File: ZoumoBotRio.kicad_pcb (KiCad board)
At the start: 2 copper layers, 89.7 x 54.9 mm, 148 parts, among them CON1 BARREL_JACK, J1 Screw_Terminal_1x05, J2 Screw_Terminal_1x05, P1 USB_OTG, P10 Analog, P11 Digital, P12 Analog, P13 Digital, P14 CONN_01X06, P2 Analog, P3 Digital, P4 Analog, P5 Digital, P6 Analog, P7 Digital, P8 Analog, P9 Digital, Q1 Q_PMOS_GDS, Q2 IR Receiver, Q3 IR Receiver, U1 ZLDO1117K50TC, U2 ATmega32U4-AU, U3 SOT361-1_2, U4 TB6612FNG, U5 TB6612FNG, Y1 16MHz

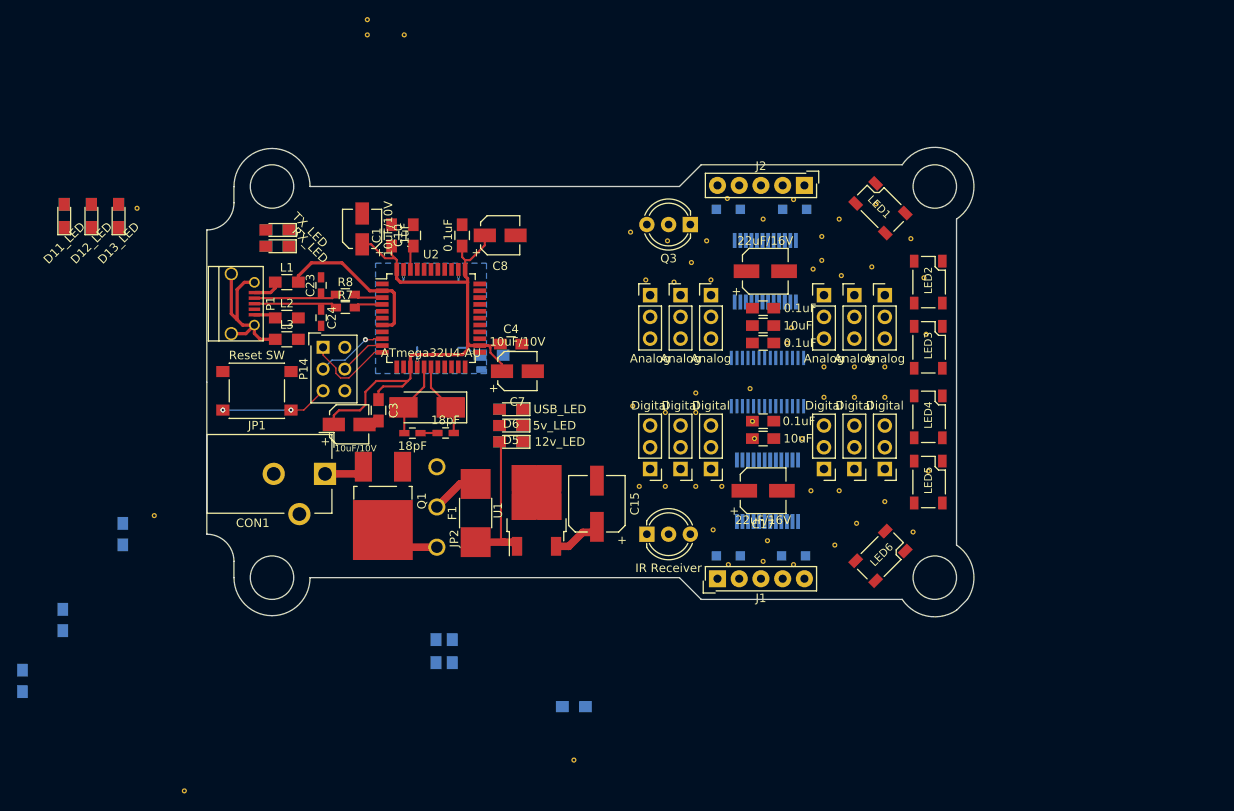
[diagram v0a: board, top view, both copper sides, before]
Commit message: Finished v2 layout, no traces
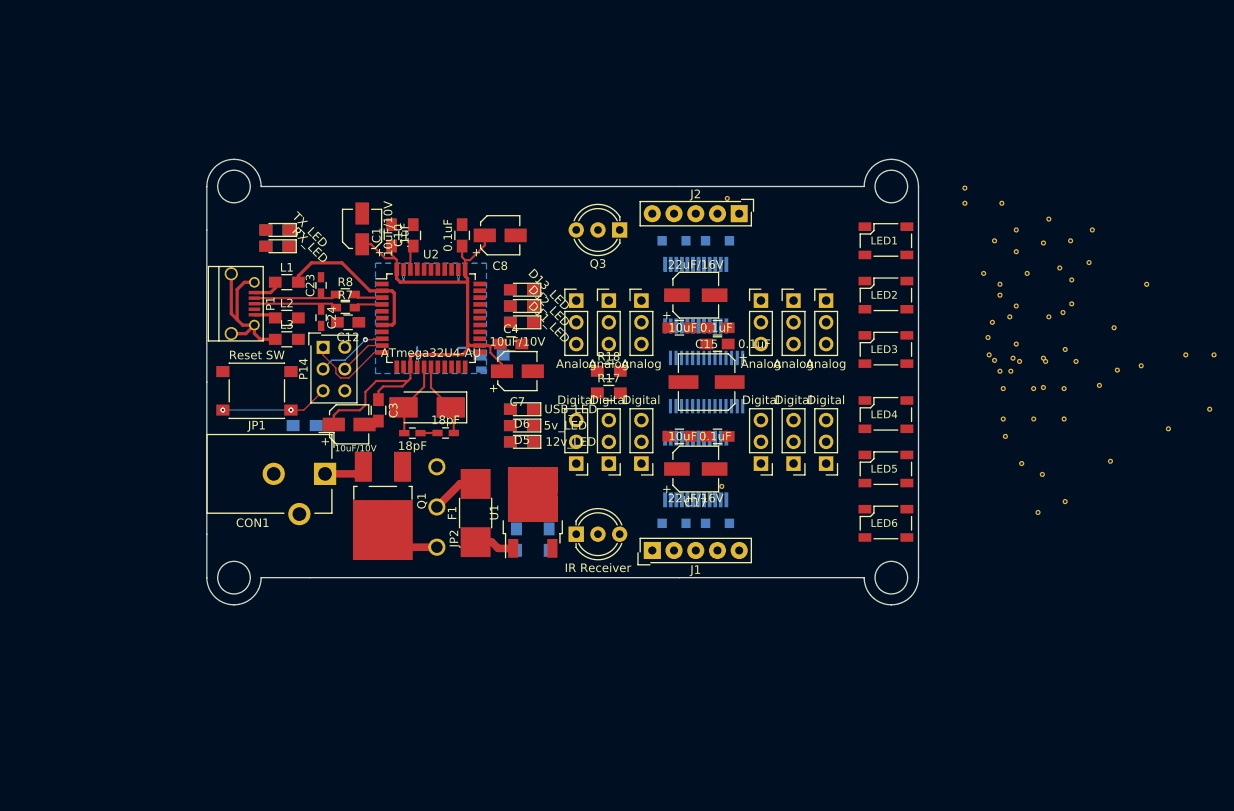
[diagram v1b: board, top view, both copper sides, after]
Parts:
- C12, R17, R18: moved to F.Cu
- moved REF** 117.0 mm to (208.5, 112.2), turned to 45 degrees
- moved REF** 111.9 mm to (209.8, 121.0)
- moved REF** 109.7 mm to (204.5, 108.0)
- moved REF** 80.9 mm to (210.2, 105.4), turned to 45 degrees
- moved REF** 72.6 mm to (197.1, 90.9)
- moved REF** 72.6 mm to (192.8, 90.9)
- moved REF** 72.6 mm to (192.8, 89.1)
- moved C14 63.7 mm to (144.1, 130.2)
- moved D4 54.9 mm to (141.0, 104.8), turned to 180 degrees
- moved R5 54.9 mm to (141.0, 104.8), turned to 180 degrees
- moved C13 53.9 mm to (140.3, 130.2)
- moved REF** 51.4 mm to (205.1, 95.2)
- moved D3 51.4 mm to (141.0, 102.9), turned to 180 degrees
- moved R4 51.4 mm to (141.0, 102.9), turned to 180 degrees
- moved REF** 49.8 mm to (213.4, 109.9)
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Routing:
- net +12V: track 16.4 -> 4.94 mm
- net +5V: track 75.2 -> 69.5 mm
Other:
- board size 89.7 x 54.9 mm -> 83.2 x 52.1 mm

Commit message: Started drawing traces
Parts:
- moved REF** 28.5 mm to (193.2, 94.6)
- moved R18 2.54 mm to (151.2, 113.0)
- moved D2 2.54 mm to (141.0, 98.4)
- moved R3 2.54 mm to (141.0, 98.4)
- moved R17 1.91 mm to (151.2, 111.1)
- moved D3 1.27 mm to (141.0, 101.6)
- moved R4 1.27 mm to (141.0, 101.6)
- moved D1 1.27 mm to (141.0, 120.0)
- moved D6 1.27 mm to (141.0, 113.7)
- moved R1 1.27 mm to (141.0, 120.0)
- moved R6 1.27 mm to (141.0, 113.7)
- moved LED1 0.63 mm to (182.9, 95.2)
- moved LED2 0.63 mm to (182.9, 101.6)
- moved LED3 0.63 mm to (182.9, 108.0)
- moved LED4 0.63 mm to (182.9, 115.6)
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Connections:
- net /digitalGround renamed /dGnd
- LED6 pad 1: Net-(LED6-Pad1) -> GND
- LED6 pad 2: +5V -> Net-(LED5-Pad4)
- LED6 pad 3: Net-(LED5-Pad4) -> +5V
- LED6 pad 4: GND -> Net-(LED6-Pad4)
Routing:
- net +5V: track 69.5 -> 440.2 mm, vias 0 -> 3
- net A0: track 0.00 -> 58.4 mm, vias 0 -> 2
- net D10: track 0.00 -> 56.1 mm, vias 0 -> 4
- net A1: track 0.00 -> 56.1 mm, vias 0 -> 2
- net D0/RXI: track 0.00 -> 51.8 mm
- net A2: track 0.00 -> 51.7 mm, vias 0 -> 2
- net Net-(R11-Pad2): track 0.00 -> 48.7 mm, vias 0 -> 1
- net D4: track 0.00 -> 46.6 mm, vias 0 -> 2
- net D1/TXO: track 0.00 -> 45.6 mm, vias 0 -> 1
- net /SCL/D3: track 0.00 -> 41.7 mm, vias 0 -> 5
- net UVcc: track 19.1 -> 60.8 mm, vias 0 -> 4
- net A3: track 0.00 -> 40.3 mm, vias 0 -> 2
- net /SDA/D2: track 0.00 -> 38.2 mm, vias 0 -> 5
- net D7: track 0.00 -> 37.4 mm, vias 0 -> 2
- net Net-(R10-Pad2): track 0.00 -> 34.5 mm, vias 0 -> 1
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- added copper zone on B.Cu, net /dGnd
- removed copper zone on B.Cu, net dGnd

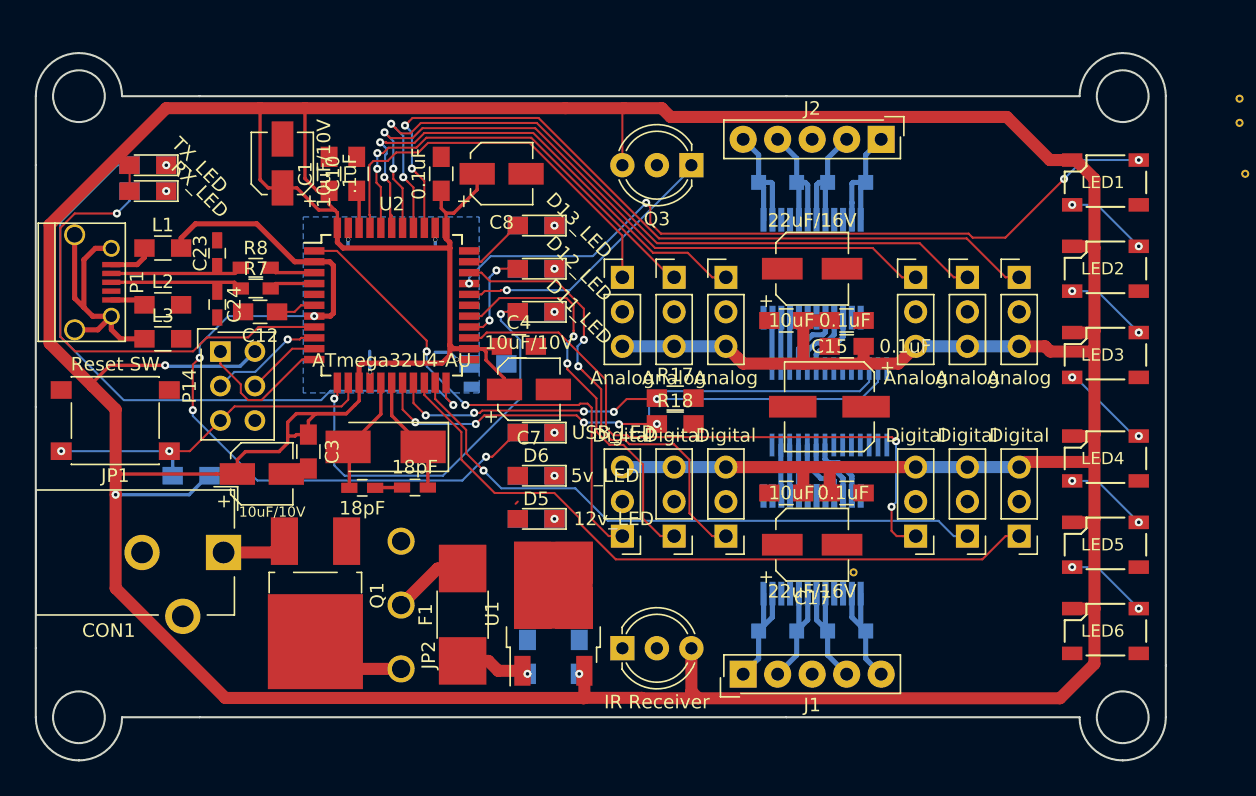
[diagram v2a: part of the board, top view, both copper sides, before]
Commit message: Continued laying out traces and copper pour
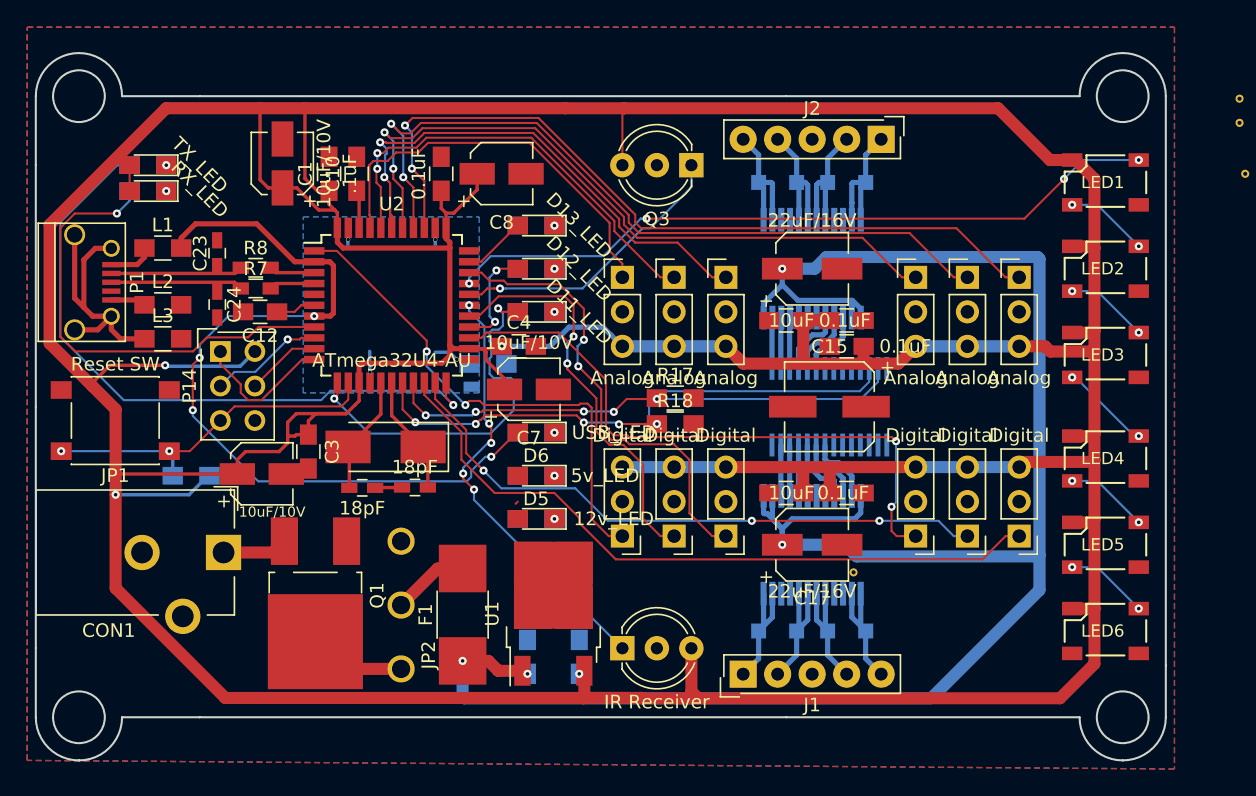
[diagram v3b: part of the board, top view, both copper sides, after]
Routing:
- net +12V: track 5.17 -> 145.0 mm, vias 1 -> 4
- net D8: track 0.00 -> 31.8 mm, vias 0 -> 5
- net +5V: track 440.2 -> 450.9 mm, vias 3 -> 4
- net D11: track 30.7 -> 27.7 mm
- net D10: track 56.1 -> 53.3 mm
- net D9: track 20.4 -> 21.2 mm
- net D12: track 7.22 -> 7.85 mm
- net D1/TXO: vias 1 -> 3
- added copper zone on B.Cu, net GND
- added copper zone on F.Cu, net GND

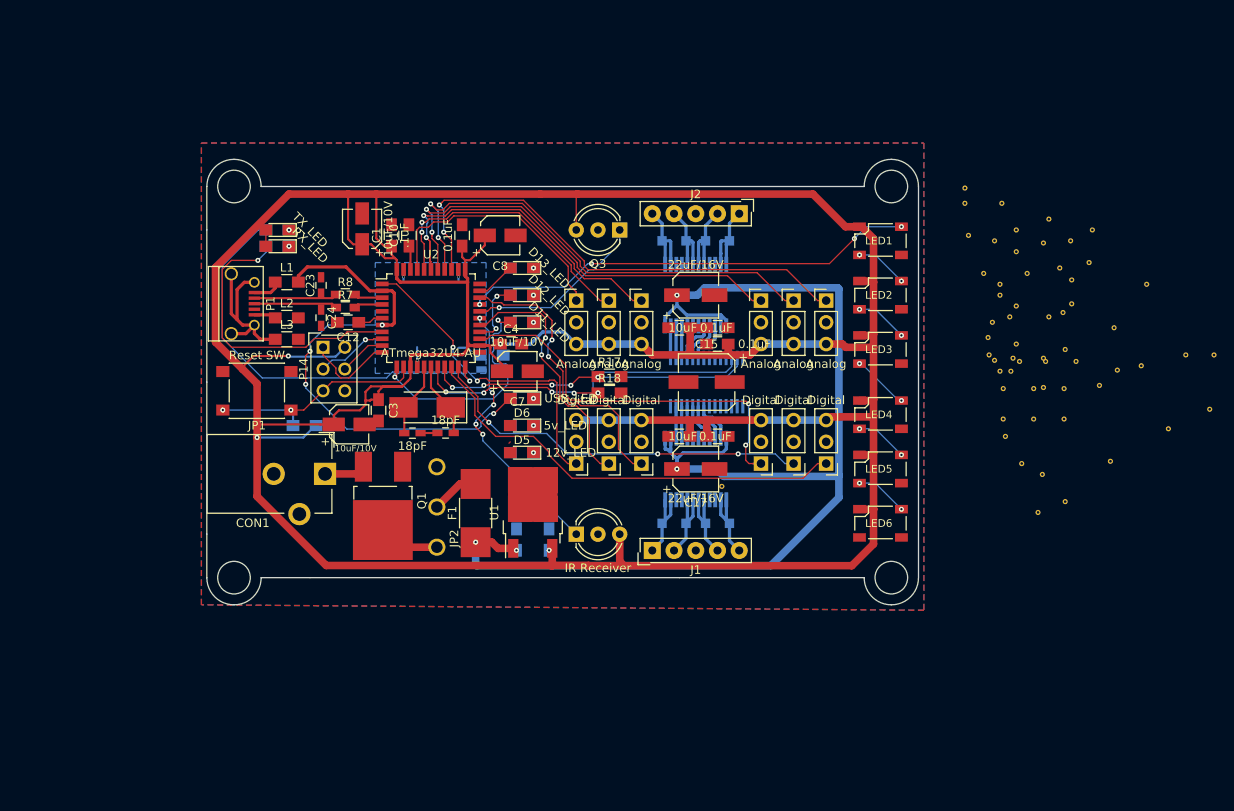
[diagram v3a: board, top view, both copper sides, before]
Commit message: Finished running traces and copper pour.
I don't know how to do a nested copper pour zones, so the dGnd plane isn't implemented correctly, and isn't connected to the pads atmega gnd pads.
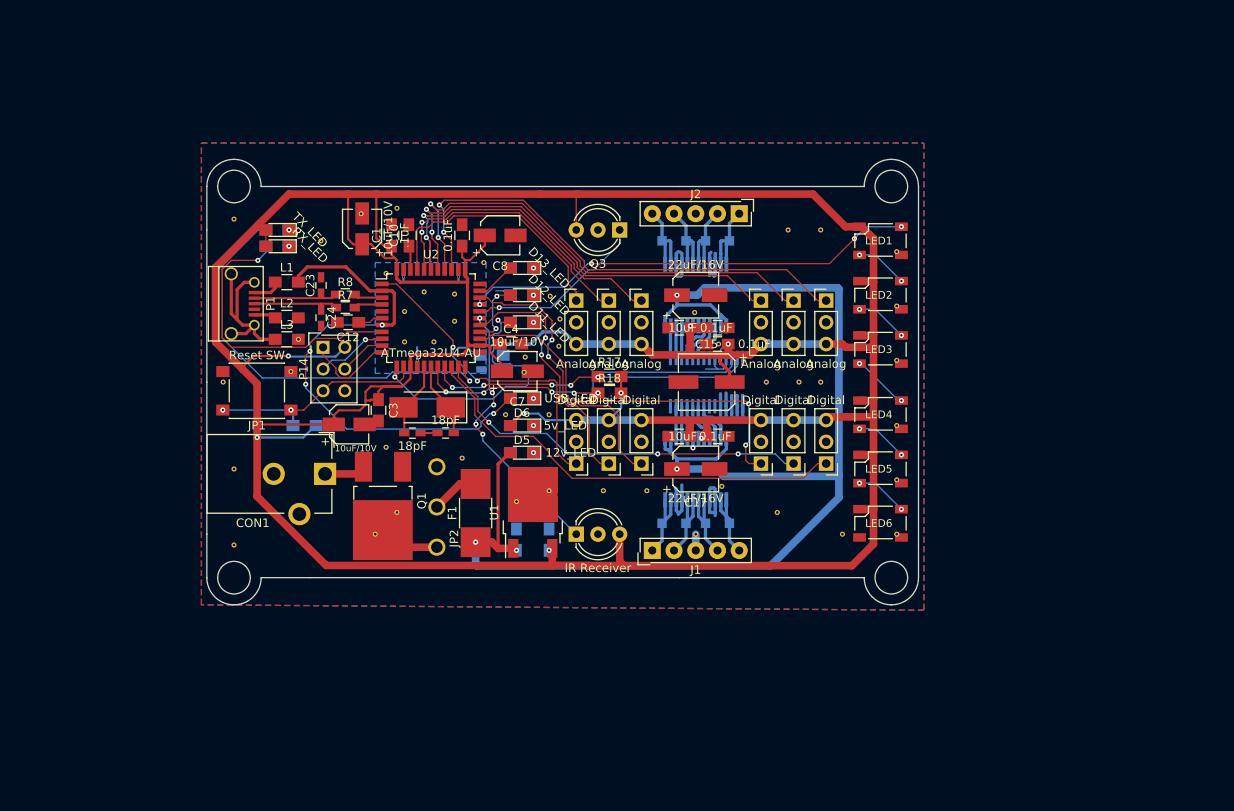
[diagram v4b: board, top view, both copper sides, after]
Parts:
- removed the REF** at (218.6, 108.6)
- removed the REF** at (216.5, 117.2)
- removed the REF** at (210.6, 110.4)
- removed the REF** at (213.4, 109.9)
- removed the REF** at (201.9, 95.5)
- removed the REF** at (221.4, 114.9)
- removed the REF** at (207.6, 94.0)
- removed the REF** at (207.3, 97.8)
- removed the REF** at (205.2, 99.8)
- removed the REF** at (214.0, 100.3)
- removed the REF** at (204.2, 103.6)
- removed the REF** at (205.2, 102.6)
- removed the REF** at (202.6, 92.7)
- removed the REF** at (205.1, 95.2)
- removed the REF** at (197.1, 90.9)
- removed the REF** at (210.2, 105.4)
- removed the REF** at (221.9, 108.6)
- added REF**: VIA-.6mm, VIA:VIA-.6mm, F.Cu at (145.3, 107.6)
- added REF**: VIA-.6mm, VIA:VIA-.6mm, F.Cu at (145.4, 104.4)
- added REF**: VIA-.6mm, VIA:VIA-.6mm, F.Cu at (144.3, 101.7)
- added REF**: VIA-.6mm, VIA:VIA-.6mm, F.Cu at (164.0, 107.3)
- added REF**: VIA-.6mm, VIA:VIA-.6mm, F.Cu at (122.2, 92.1)
- added REF**: VIA-.6mm, VIA:VIA-.6mm, F.Cu at (141.2, 110.6)
- added REF**: VIA-.6mm, VIA:VIA-.6mm, F.Cu at (114.0, 110.5)
- moved REF** 99.8 mm to (107.3, 92.7)
- moved REF** 94.8 mm to (107.3, 130.8)
- moved REF** 92.0 mm to (107.3, 121.9)
- moved REF** 89.2 mm to (106.0, 111.8)
- moved REF** 79.9 mm to (114.8, 106.8)
- moved REF** 78.7 mm to (117.5, 95.2)
- moved REF** 78.4 mm to (123.8, 129.5)
- moved REF** 75.0 mm to (126.4, 127.0)
- moved REF** 73.7 mm to (125.1, 99.1)
- moved REF** 73.3 mm to (126.4, 91.4)
- moved REF** 72.2 mm to (125.1, 119.4)
- moved REF** 68.2 mm to (127.3, 107.1)
- moved REF** 67.3 mm to (129.5, 101.2)
- moved REF** 67.0 mm to (139.1, 115.6)
- moved REF** 66.8 mm to (136.5, 97.8)
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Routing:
- net GND: track 1.99 -> 55.1 mm, vias 0 -> 1
- net +5V: track 450.9 -> 476.2 mm, vias 4 -> 9
- net +12V: track 145.0 -> 156.9 mm
- net D11: track 27.7 -> 32.4 mm
- net D+: track 13.1 -> 13.8 mm
- net D-: track 13.1 -> 13.6 mm
